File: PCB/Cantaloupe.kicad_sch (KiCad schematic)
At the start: 8 parts

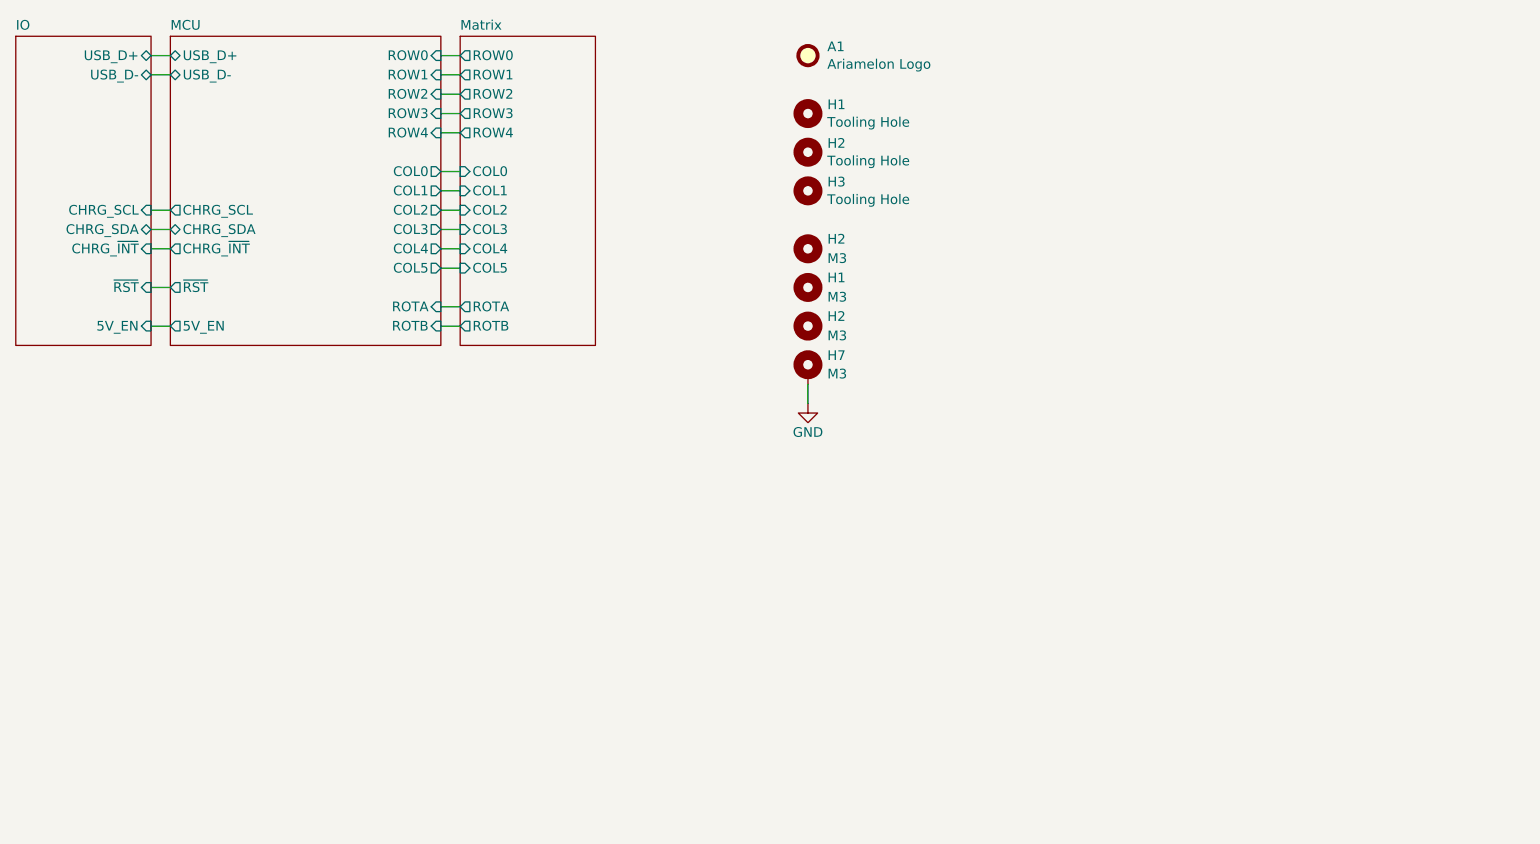
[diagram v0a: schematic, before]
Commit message: 24/08/2023 update
Finished routing. Consolidated all libraries into Ariamelon's Kicad Master Library. Added PCM12 switch connected to nPM1300 GPIO. Rearranged components and rerouted.
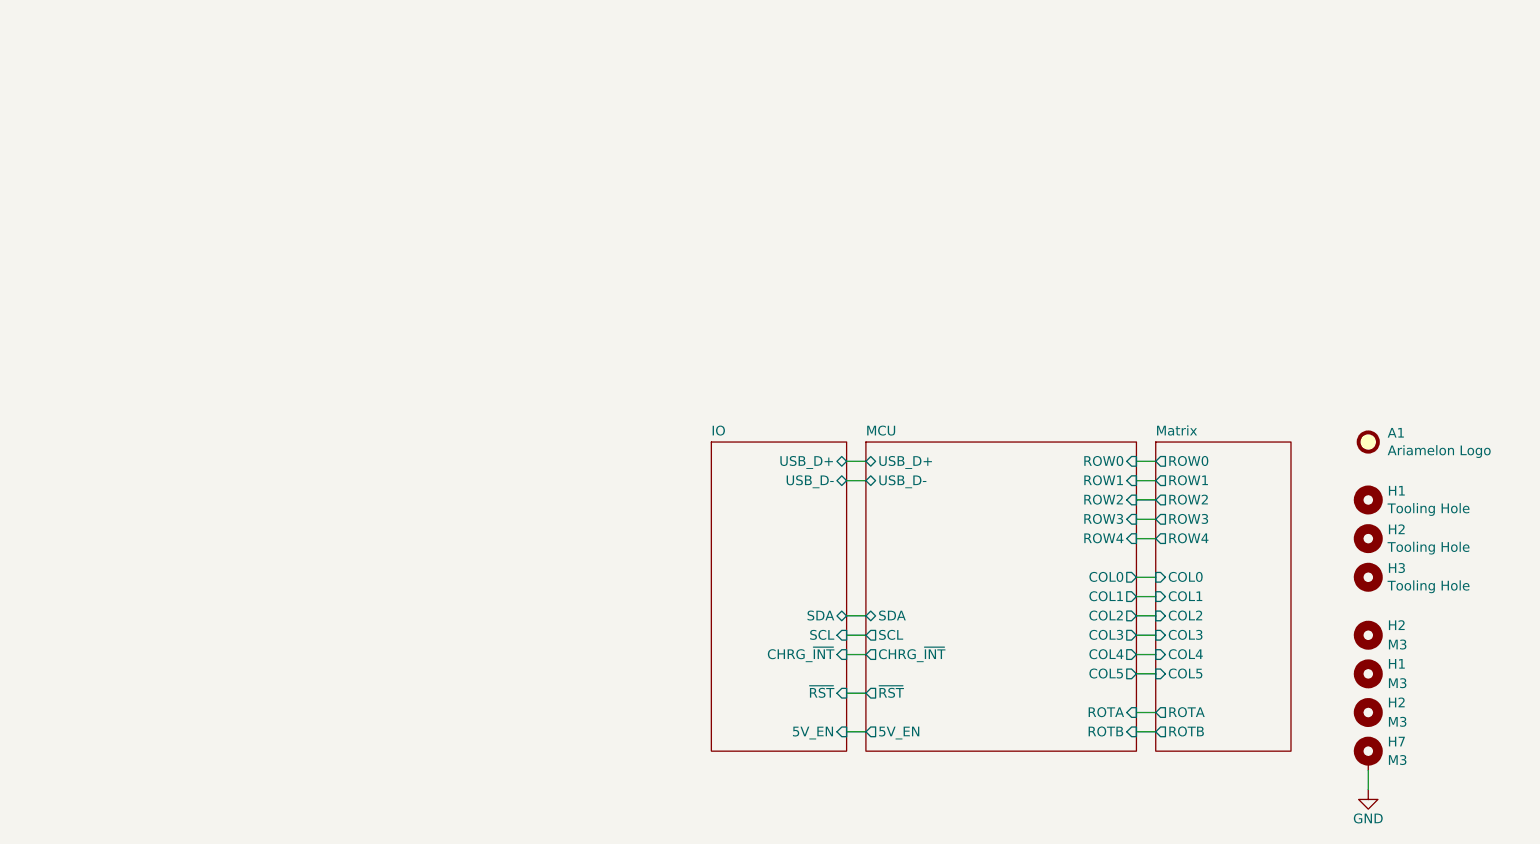
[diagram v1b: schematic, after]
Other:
- sheet IO ports: added SCL, SDA; removed CHRG_SCL, CHRG_SDA
- sheet MCU ports: added SCL, SDA; removed CHRG_SCL, CHRG_SDA
- moved on the sheet: A1, H1, H2, H3, H7

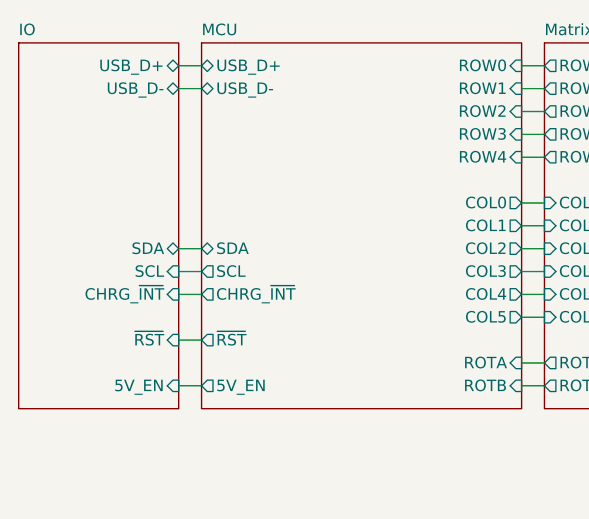
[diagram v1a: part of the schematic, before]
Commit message: Cantaloupe V3.0 name changed to CantaloupeBT V1.0 ('BT-V1' branch). Key features updated. Design will be reworked in the coming days!
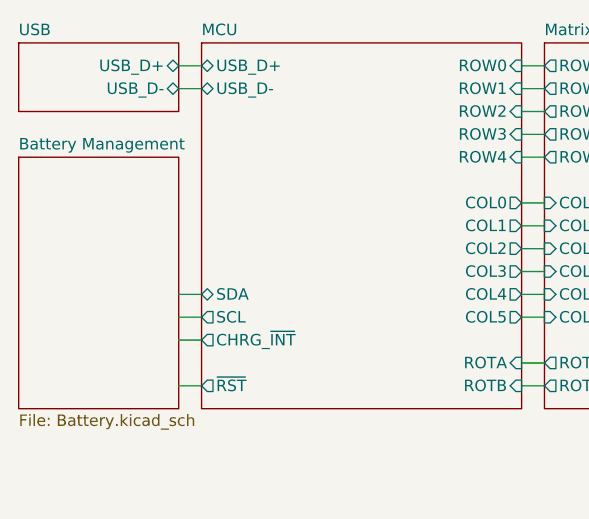
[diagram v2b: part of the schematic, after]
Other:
- sheet IO renamed USB
- added sheet Battery Management (Battery.kicad_sch)
- sheet MCU ports: added none; removed 5V_EN
- sheet USB: file IO.kicad_sch -> USB.kicad_sch
- sheet USB ports: added none; removed 5V_EN, CHRG_~{INT}, SCL, SDA, ~{RST}
- title: Cantaloupe split ergonomic keyboard -> CantaloupeLP split ergonomic keyboard
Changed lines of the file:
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@@
   (paper "A4")
   (title_block
-    (title "Cantaloupe split ergonomic keyboard")
-    (date "2023-08-22")
-    (rev "V3.0")
+    (title "CantaloupeLP split ergonomic keyboard")
+    (date "2024-10-16")
+    (rev "V1.0")
     (company "Created by Ariamelon (https://github.com/Ariamelon/Cantaloupe/)")
     (comment 1 "Follows the VIK standard by Sadek Baroudi (https://github.com/sadekbaroudi/VIK)")
@@
     (stroke (width 0) (type default))
   )
-  (wire (pts (xy 129.54 93.98) (xy 127 93.98))
+  (wire (pts (xy 129.54 99.06) (xy 127 99.06))
     (stroke (width 0) (type default))
   )
@@
     (stroke (width 0) (type default))
   )
-  (wire (pts (xy 129.54 96.52) (xy 127 96.52))
+  (wire (pts (xy 129.54 101.6) (xy 127 101.6))
     (stroke (width 0) (type default))
   )
@@
     (stroke (width 0) (type default))
   )
+  (wire (pts (xy 127 73.66) (xy 129.54 73.66))
+    (stroke (width 0) (type default))
+  )
+  (wire (pts (xy 127 76.2) (xy 129.54 76.2))
+    (stroke (width 0) (type default))
+  )
   (wire (pts (xy 129.54 109.22) (xy 127 109.22))
     (stroke (width 0) (type default))
   )
-  (wire (pts (xy 127 73.66) (xy 129.54 73.66))
-    (stroke (width 0) (type default))
-  )
-  (wire (pts (xy 127 76.2) (xy 129.54 76.2))
+  (wire (pts (xy 165.1 96.52) (xy 167.64 96.52))
+    (stroke (width 0) (type default))
+  )
+  (wire (pts (xy 165.1 73.66) (xy 167.64 73.66))
+    (stroke (width 0) (type default))
+  )
+  (wire (pts (xy 167.64 99.06) (xy 165.1 99.06))
+    (stroke (width 0) (type default))
+  )
+  (wire (pts (xy 165.1 81.28) (xy 167.64 81.28))
     (stroke (width 0) (type default))
   )
   (wire (pts (xy 129.54 104.14) (xy 127 104.14))
-    (stroke (width 0) (type default))
-  )
-  (wire (pts (xy 165.1 96.52) (xy 167.64 96.52))
-    (stroke (width 0) (type default))
-  )
-  (wire (pts (xy 165.1 73.66) (xy 167.64 73.66))
-    (stroke (width 0) (type default))
-  )
-  (wire (pts (xy 167.64 99.06) (xy 165.1 99.06))
-    (stroke (width 0) (type default))
-  )
-  (wire (pts (xy 165.1 81.28) (xy 167.64 81.28))
-    (stroke (width 0) (type default))
-  )
-  (wire (pts (xy 129.54 99.06) (xy 127 99.06))
     (stroke (width 0) (type default))
   )
@@
           (reference "#PWR01") (unit 1)
         )
-        (path "/534caec7-cf60-4f90-b1ed-42c9d445ef0f/d133c1c6-f35d-4b98-81a0-3607ab1d2de1"
-          (reference "#PWR014") (unit 1)
-        )
       )
     )
@@
     )
   )
-  (sheet (at 109.22 71.12) (size 17.78 40.64) (fields_autoplaced)
+  (sheet (at 109.22 71.12) (size 17.78 7.62) (fields_autoplaced)
     (stroke (width 0.1524) (type solid))
     (fill (color 0 0 0 0.0000))
-    (property "Sheetname" "IO" (at 109.22 70.4084 0)
+    (property "Sheetname" "USB" (at 109.22 70.4084 0)
       (effects (font (size 1.27 1.27)) (justify left bottom))
     )
-    (property "Sheetfile" "IO.kicad_sch" (at 109.22 112.3446 0)
+    (property "Sheetfile" "USB.kicad_sch" (at 109.22 79.3246 0)
       (effects (font (size 1.27 1.27)) (justify left top) hide)
     )
-    (pin "5V_EN" input (at 127 109.22 0)
-      (effects (font (size 1.27 1.27)) (justify right))
-    )
-    (pin "~{RST}" input (at 127 104.14 0)
-      (effects (font (size 1.27 1.27)) (justify right))
-    )
-    (pin "CHRG_~{INT}" input (at 127 99.06 0)
-      (effects (font (size 1.27 1.27)) (justify right))
+    (property "Field2" "" (at 109.22 71.12 0)
+      (effects (font (size 1.27 1.27)) hide)
     )
     (pin "USB_D-" bidirectional (at 127 76.2 0)
@@
       (effects (font (size 1.27 1.27)) (justify right))
     )
-    (pin "SDA" bidirectional (at 127 93.98 0)
-      (effects (font (size 1.27 1.27)) (justify right))
-    )
-    (pin "SCL" input (at 127 96.52 0)
-      (effects (font (size 1.27 1.27)) (justify right))
-    )
     (instances
       (project "Cantaloupe"
         (path "/534caec7-cf60-4f90-b1ed-42c9d445ef0f" (page "6"))
+      )
+    )
+  )
+  (sheet (at 109.22 83.82) (size 17.78 27.94) (fields_autoplaced)
+    (stroke (width 0.1524) (type solid))
+    (fill (color 0 0 0 0.0000))
+    (property "Sheetname" "Battery Management" (at 109.22 83.1084 0)
+      (effects (font (size 1.27 1.27)) (justify left bottom))
+    )
+    (property "Sheetfile" "Battery.kicad_sch" (at 109.22 112.3446 0)
+      (effects (font (size 1.27 1.27)) (justify left top))
+    )
+    (instances
+      (project "Cantaloupe"
+        (path "/534caec7-cf60-4f90-b1ed-42c9d445ef0f" (page "5"))
       )
     )
@@
       (effects (font (size 1.27 1.27)) (justify right))
     )
-    (pin "~{RST}" output (at 129.54 104.14 180)
-      (effects (font (size 1.27 1.27)) (justify left))
-    )
-    (pin "CHRG_~{INT}" output (at 129.54 99.06 180)
-      (effects (font (size 1.27 1.27)) (justify left))
-    )
-    (pin "5V_EN" output (at 129.54 109.22 180)
-      (effects (font (size 1.27 1.27)) (justify left))
-    )
-    (pin "SDA" bidirectional (at 129.54 93.98 180)
-      (effects (font (size 1.27 1.27)) (justify left))
-    )
-    (pin "SCL" output (at 129.54 96.52 180)
-      (effects (font (size 1.27 1.27)) (justify left))
-    )
+    (pin "~{RST}" output (at 129.54 109.22 180)
+      (effects (font (size 1.27 1.27)) (justify left))
+    )
+    (pin "CHRG_~{INT}" output (at 129.54 104.14 180)
+      (effects (font (size 1.27 1.27)) (justify left))
+    )
+    (pin "SDA" bidirectional (at 129.54 99.06 180)
+      (effects (font (size 1.27 1.27)) (justify left))
+    )
+    (pin "SCL" output (at 129.54 101.6 180)
+      (effects (font (size 1.27 1.27)) (justify left))
+    )
